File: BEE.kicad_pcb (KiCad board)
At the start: 2 copper layers, 77.5 x 40 mm, 40 parts, among them J1 RPI1_header, J10 Conn_01x02, J11 Conn_01x02, J12 Conn_01x02, J13 Conn_01x06, J14 Conn_01x03, J15 Conn_01x03, J16 Conn_01x08, J17 Conn_01x03, J2 Conn_02x05_Odd_Even, J3 Conn_02x03_Odd_Even, J4 Conn_01x06, J5 Conn_02x10_Odd_Even, J6 Conn_02x02_Odd_Even, J7 Conn_02x02_Odd_Even, J8 Conn_01x08, J9 Conn_01x02, SW1 SW_Push, SW2 SW_Push, SW3 SW_Push, U1 MCP3008, U2 MCP4911

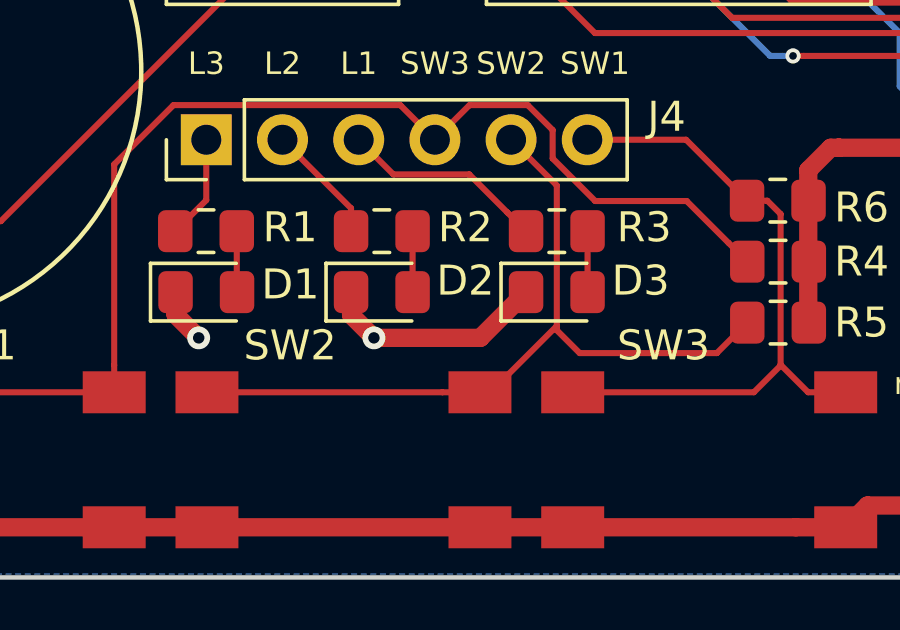
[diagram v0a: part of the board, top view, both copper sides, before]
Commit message: additional via for led circuits
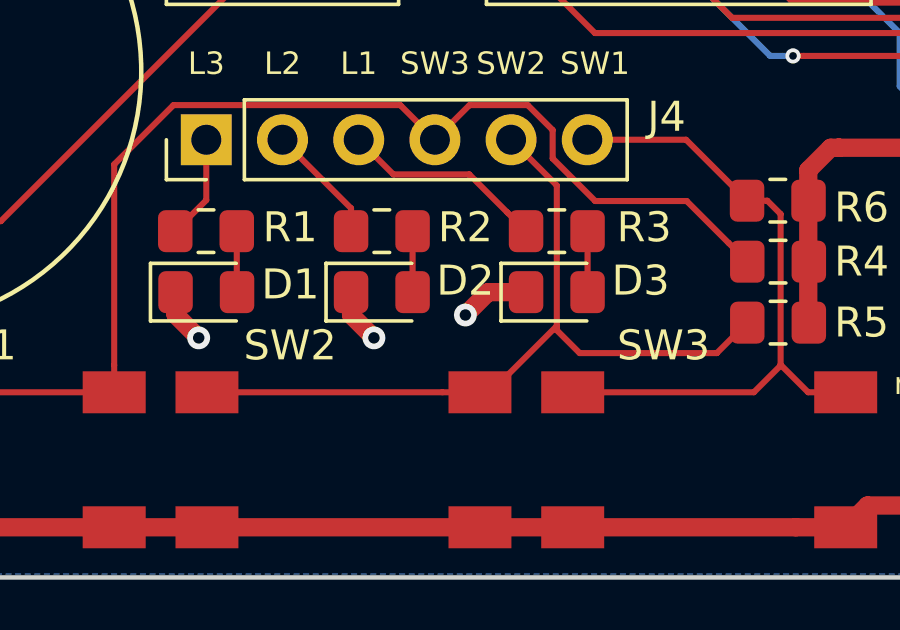
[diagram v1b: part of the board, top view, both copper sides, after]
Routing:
- net GND: track 62.4 -> 59.0 mm, vias 6 -> 7
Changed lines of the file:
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@@
     (thickness 1.6)
     (drawings 63)
-    (tracks 430)
+    (tracks 431)
     (zones 0)
     (modules 40)
@@
   (segment (start 115.307 110.49) (end 115.307 111.243) (width 0.6096) (layer F.Cu) (net 3))
   (segment (start 115.307 111.243) (end 116.078 112.014) (width 0.6096) (layer F.Cu) (net 3))
-  (via (at 121.92 112.014) (size 0.762) (drill 0.381) (layers F.Cu B.Cu) (net 3))
-  (segment (start 121.158 110.49) (end 121.158 111.252) (width 0.6096) (layer F.Cu) (net 3))
-  (segment (start 121.158 111.252) (end 121.92 112.014) (width 0.6096) (layer F.Cu) (net 3))
-  (segment (start 125.467 112.014) (end 121.92 112.014) (width 0.6096) (layer F.Cu) (net 3))
-  (segment (start 126.991 110.49) (end 125.467 112.014) (width 0.6096) (layer F.Cu) (net 3))
   (segment (start 146.091761 114.594081) (end 145.028488 114.594081) (width 0.6096) (layer F.Cu) (net 3))
   (via (at 145.028488 114.594081) (size 0.762) (drill 0.381) (layers F.Cu B.Cu) (net 3))
   (segment (start 146.685 113.19) (end 146.685 114.000842) (width 0.6096) (layer F.Cu) (net 3))
   (segment (start 146.685 114.000842) (end 146.091761 114.594081) (width 0.6096) (layer F.Cu) (net 3))
+  (via (at 121.92 112.014) (size 0.762) (drill 0.381) (layers F.Cu B.Cu) (net 3))
+  (segment (start 121.158 110.49) (end 121.158 111.252) (width 0.6096) (layer F.Cu) (net 3))
+  (segment (start 121.158 111.252) (end 121.92 112.014) (width 0.6096) (layer F.Cu) (net 3))
+  (via (at 124.968 111.252) (size 0.762) (drill 0.381) (layers F.Cu B.Cu) (net 3))
+  (segment (start 126.991 110.49) (end 125.73 110.49) (width 0.6096) (layer F.Cu) (net 3))
+  (segment (start 125.73 110.49) (end 124.968 111.252) (width 0.6096) (layer F.Cu) (net 3))
   (segment (start 117.348 110.481) (end 117.357 110.49) (width 0.2032) (layer F.Cu) (net 4))
   (segment (start 117.348 108.458) (end 117.348 110.481) (width 0.2032) (layer F.Cu) (net 4))

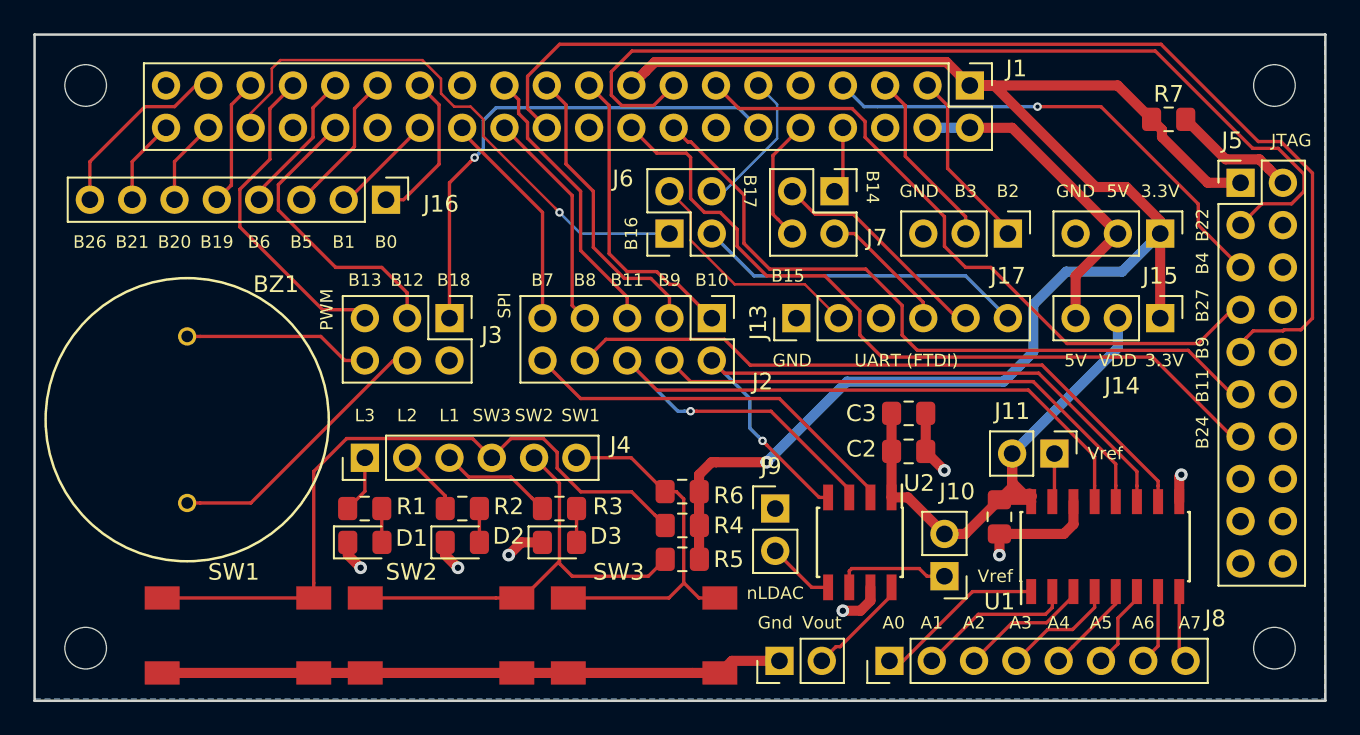
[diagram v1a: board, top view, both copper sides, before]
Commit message: reposition, reroute, removed cross connector for UART. Labeled
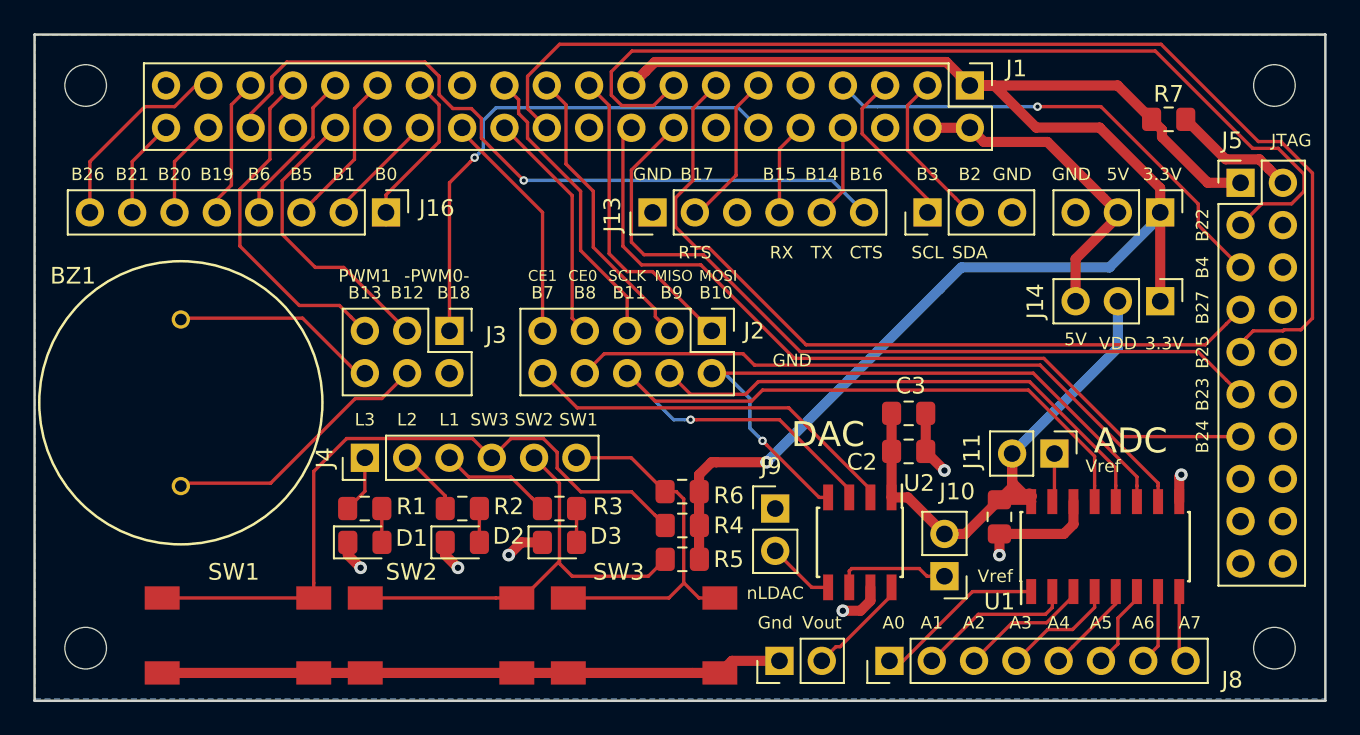
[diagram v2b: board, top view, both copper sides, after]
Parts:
- removed J6, J7: Conn_02x02_Odd_Even, Connector_PinHeader_2.54mm:PinHeader_2x02_P2.54mm_Vertical
- moved J13 10.7 mm to (133.6, 90.7)
- moved J17 4.99 mm to (150.1, 90.7), turned to 90 degrees
- moved J15 1.27 mm to (164.1, 90.7)
- moved BZ1 1.09 mm to (105.3, 102.1)
- moved J14 1.02 mm to (164.1, 96.0)
- moved J16 0.76 mm to (117.6, 90.7)
- moved J2 0.76 mm to (137.2, 97.8)
- moved J3 0.76 mm to (121.4, 97.8)
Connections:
- J1 pad 11: /BCM17_RTS1 -> /BCM17_RTS
- J1 pad 36: /BCM16_CTS1 -> /BCM16_CTS
- J13 pad 2: Net-(J13-Pad2) -> /BCM17_RTS
- J13 pad 4: Net-(J13-Pad4) -> /BCM15_RX
- J13 pad 5: Net-(J13-Pad5) -> /BCM14_TX
- J13 pad 6: Net-(J13-Pad6) -> /BCM16_CTS
- J17 pad 1: /BCM2_SDA -> /BCM3_SCL
- J17 pad 2: /BCM3_SCL -> /BCM2_SDA
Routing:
- net /BCM16_CTS: track 0.00 -> 44.6 mm, vias 0 -> 1
- net /BCM16_CTS1: track 33.6 -> 0.00 mm, vias 1 -> 0
- net Net-(J13-Pad6): track 19.9 -> 0.00 mm
- net Net-(J13-Pad2): track 14.3 -> 0.00 mm
- net Net-(J13-Pad5): track 13.6 -> 0.00 mm
- net /BCM17_RTS: track 0.00 -> 9.35 mm
- net /BCM17_RTS1: track 8.89 -> 0.00 mm
- net Net-(J13-Pad4): track 8.50 -> 0.00 mm
- net /BCM27_TMS: track 40.4 -> 47.2 mm
- net /BCM23_RTCK: track 43.4 -> 48.3 mm
- net /BCM24_TDO: track 47.2 -> 49.1 mm
- net /BCM15_RX: track 7.52 -> 5.61 mm
- net /BCM1: track 6.36 -> 8.24 mm
- net Net-(BZ1-Pad2): track 11.3 -> 12.8 mm
- net /BCM5: track 8.75 -> 10.3 mm
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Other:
- board text added: "-PWM0-"
- board text added: "ADC"
- board text added: "B23"
- board text added: "B25"
- board text added: "CE0"
- board text added: "CE1"
- board text added: "CTS"
- board text added: "DAC"
- board text added: "MISO"
- board text added: "MOSI"
- board text added: "PWM1"
- board text added: "RTS"
- board text added: "RX"
- board text added: "SCL"
- board text added: "SCLK"
- board text added: "SDA"
- board text added: "TX"
- board text removed: "PWM"
- board text removed: "SPI"
- board text removed: "UART (FTDI)"

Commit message: Fiducials and Logos
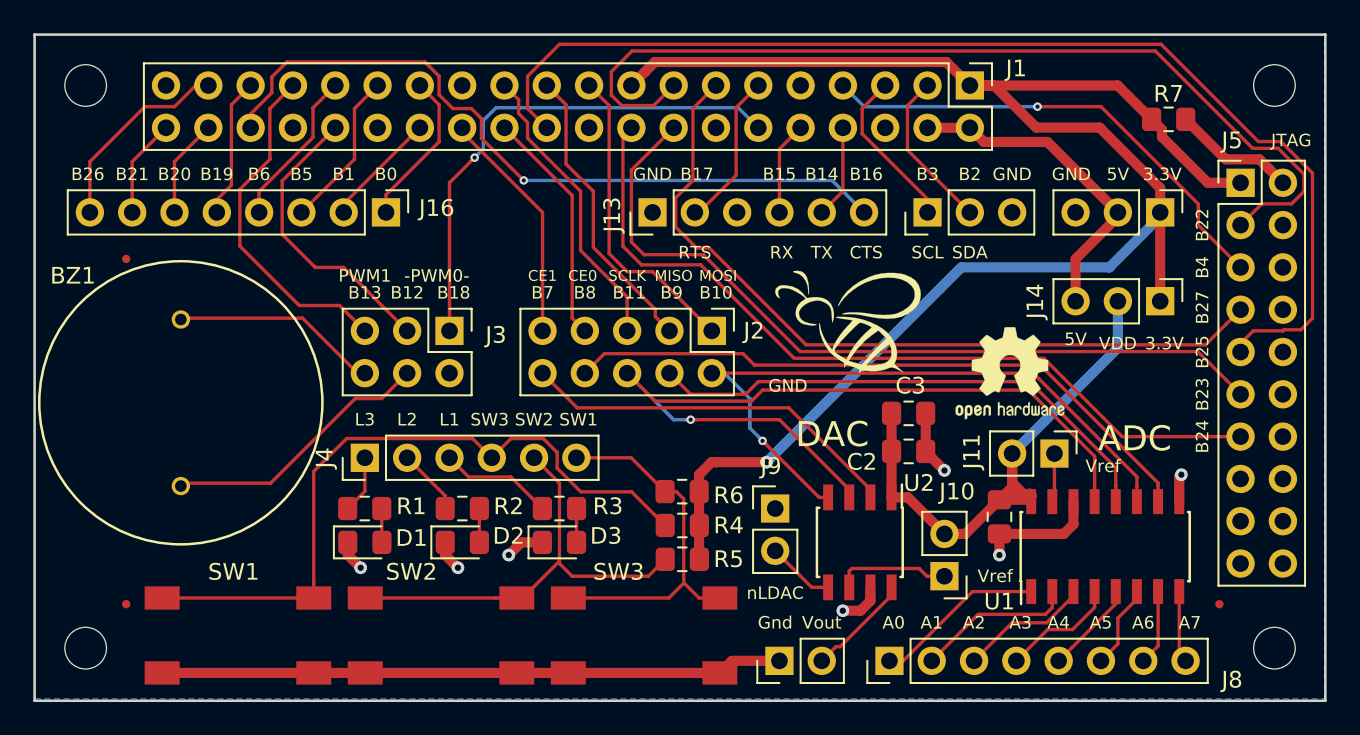
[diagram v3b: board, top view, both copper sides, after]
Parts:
- added FID1: Fiducial, Fiducial:Fiducial_0.5mm_Dia_1mm_Outer, F.Cu at (102.0, 93.5)
- added FID2: Fiducial, Fiducial:Fiducial_0.5mm_Dia_1mm_Outer, F.Cu at (102.0, 114.2)
- added FID3: Fiducial, Fiducial:Fiducial_0.5mm_Dia_1mm_Outer, F.Cu at (167.6, 114.2)
- added LOGO1: Logo_Open_Hardware_Small, Symbol:OSHW-Logo2_7.3x6mm_SilkScreen, F.Cu at (155.1, 100.3)
- added LOGO2: Logo_Open_Hardware_Small, BEElib:bee_logo, F.Cu at (145.3, 97.3)

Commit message: UCM logo and github repo url
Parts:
- added LOGO3: Logo_Open_Hardware_Small, BEElib:UCMLogo_169_169, B.Cu at (105.2, 102.4)
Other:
- board text added: "https://github.com/tenllado/bee"

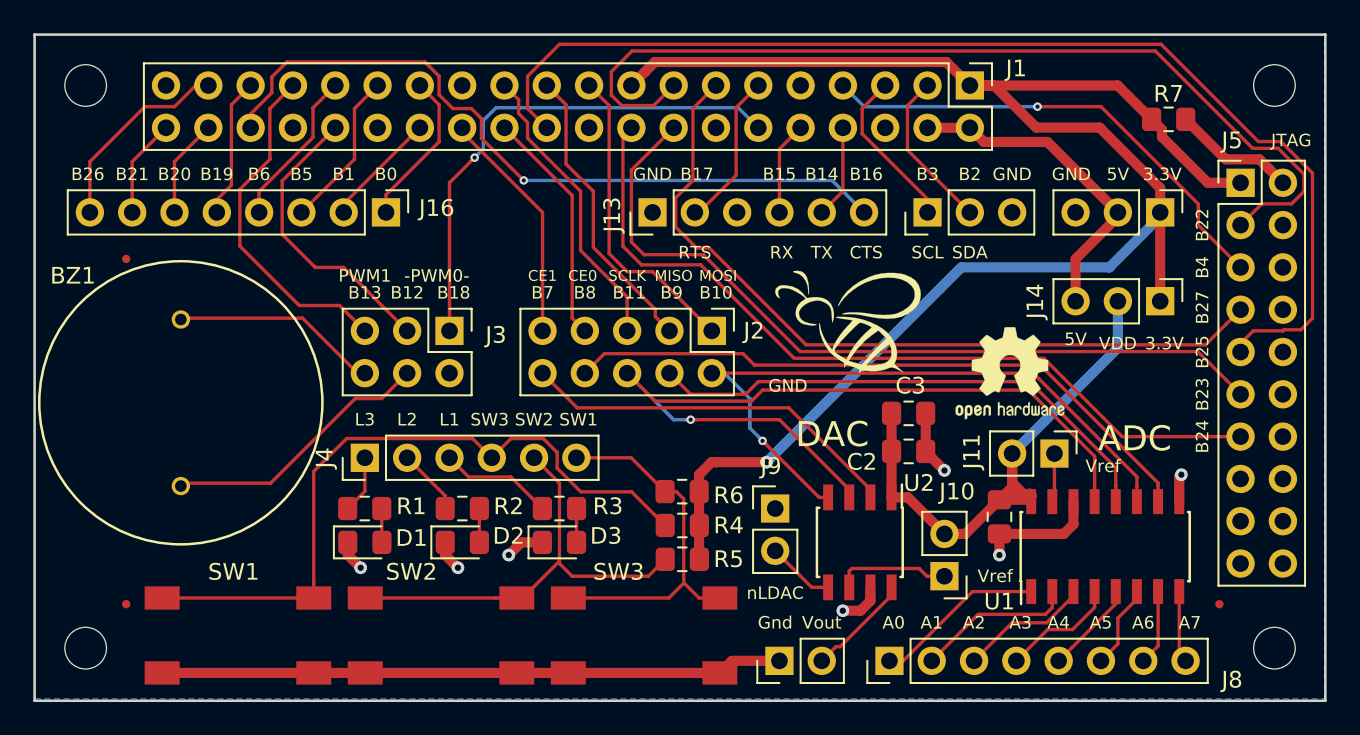
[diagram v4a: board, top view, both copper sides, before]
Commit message: some traces redone for better return path on ground plane. Reposition of fiducials.
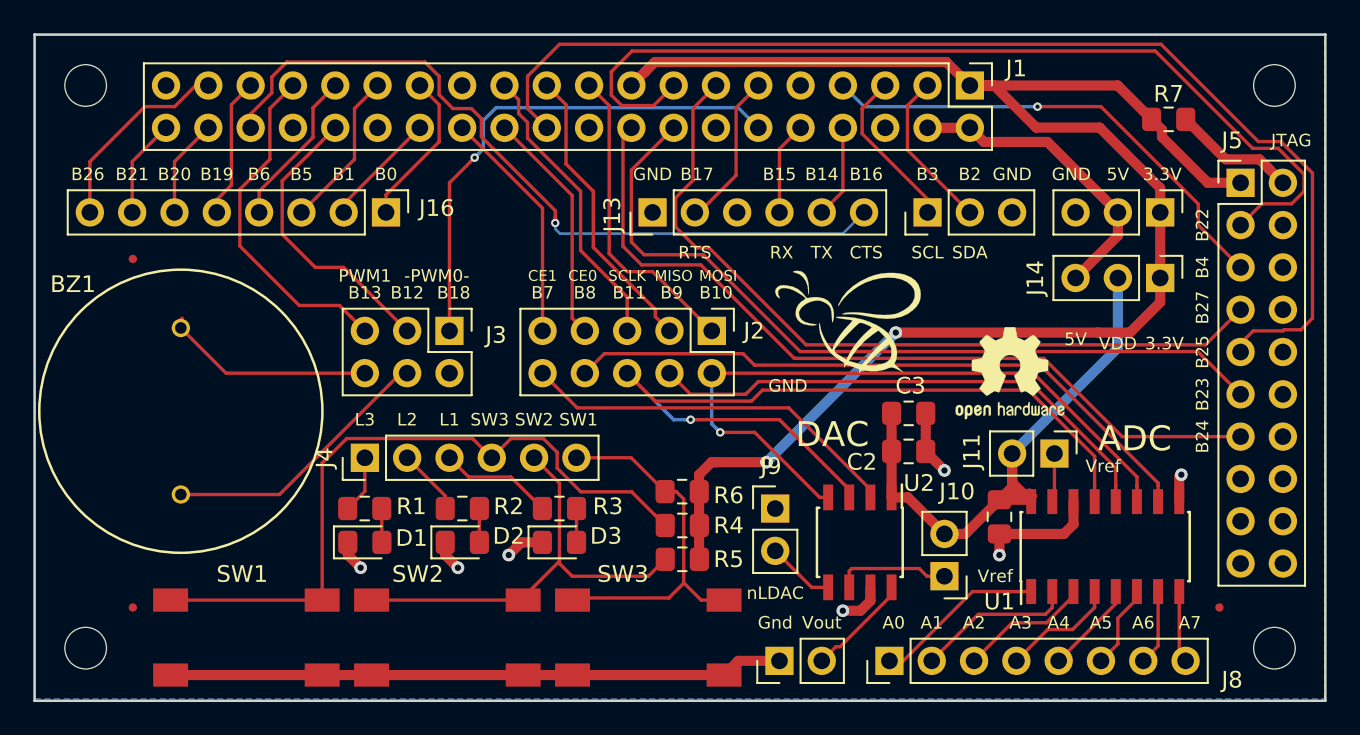
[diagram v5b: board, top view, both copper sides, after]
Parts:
- moved J14 1.40 mm to (164.1, 94.6)
- moved SW1 0.52 mm to (109.2, 116.2)
- moved BZ1 0.51 mm to (105.3, 102.6)
- moved FID2 0.45 mm to (102.4, 114.4)
- moved LOGO3 0.40 mm to (105.3, 102.7)
- moved SW2 0.40 mm to (121.3, 116.2)
- moved FID1 0.40 mm to (102.4, 93.5)
- moved SW3 0.28 mm to (133.3, 116.2)
- moved FID3 0.20 mm to (167.6, 114.4)
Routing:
- net +3V3: track 100.8 -> 98.7 mm, vias 1 -> 2
- net /BCM16_CTS: track 44.6 -> 46.2 mm
- net VDD: track 34.5 -> 35.9 mm
- net +5V: track 19.8 -> 18.5 mm
- net /MOSI: track 41.0 -> 41.8 mm
- net Net-(BZ1-Pad2): track 12.8 -> 12.3 mm

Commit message: return current loops reduced
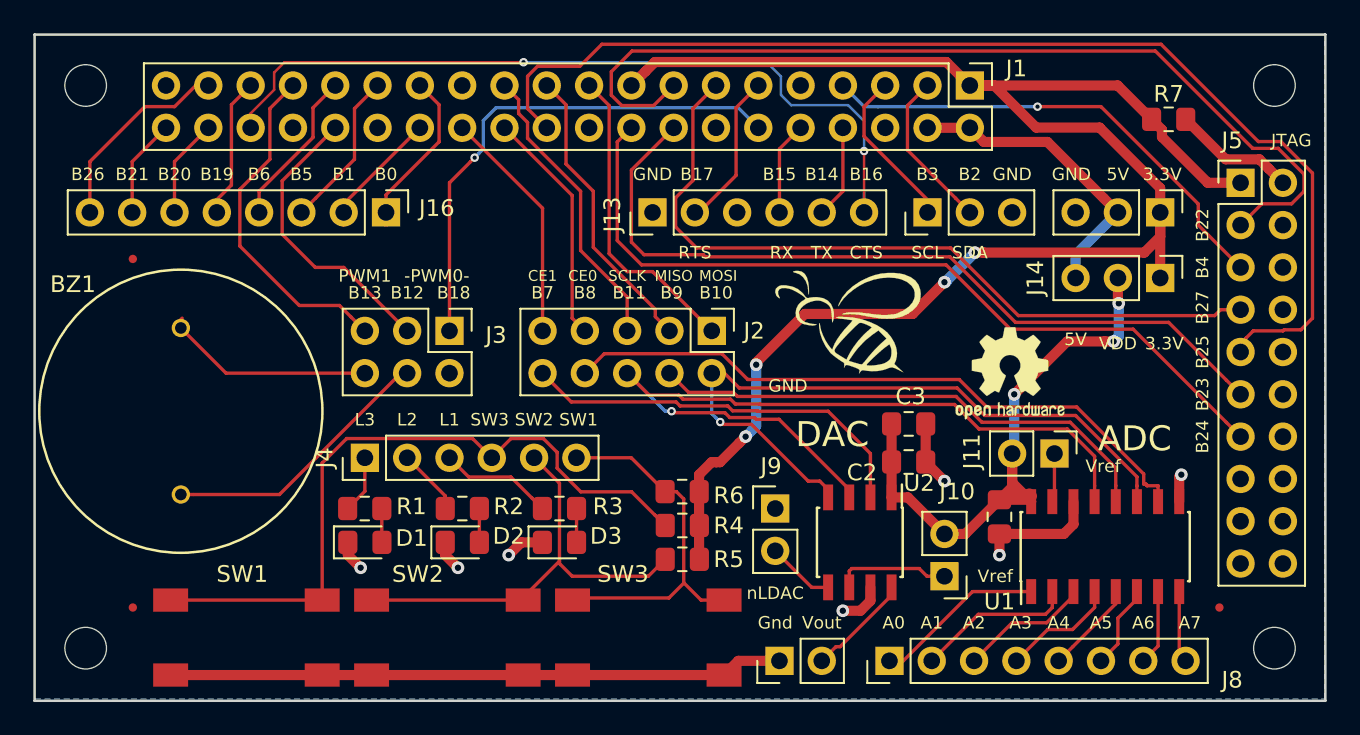
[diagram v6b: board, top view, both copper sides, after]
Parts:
- moved C2 0.64 mm to (149.0, 105.7)
- moved C3 0.64 mm to (149.0, 103.4)
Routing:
- net +3V3: track 98.7 -> 105.0 mm, vias 2 -> 4
- net /BCM16_CTS: track 46.2 -> 48.7 mm, vias 1 -> 2
- net /BCM27_TMS: track 47.2 -> 45.8 mm
- net /CE_DAC: track 23.1 -> 24.3 mm
- net VDD: track 35.9 -> 37.0 mm, vias 0 -> 3
- net /MISO: track 31.8 -> 31.2 mm
- net /SCLK: track 50.1 -> 49.6 mm

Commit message: self made logo
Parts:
- LOGO2: footprint BEElib:bee_logo -> BEElib:bee_logo2
